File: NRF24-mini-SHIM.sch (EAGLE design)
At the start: 13 parts

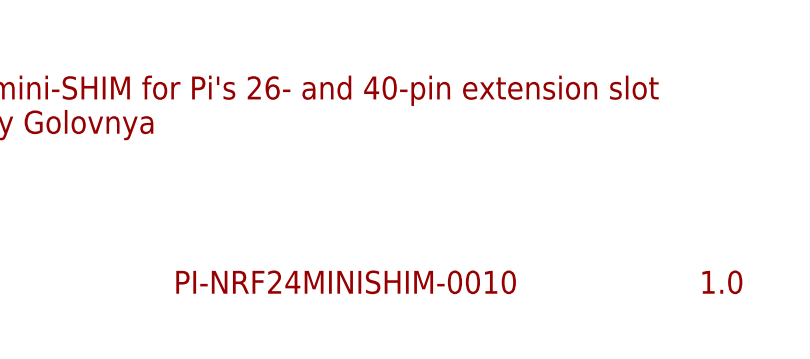
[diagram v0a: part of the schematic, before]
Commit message: Simplified document names. Generated PDF schematics.
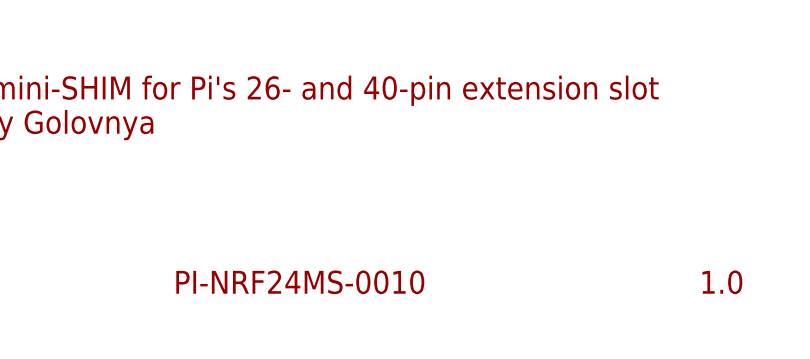
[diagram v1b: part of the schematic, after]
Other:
- note added: "PI-NRF24MS-0010"
- note removed: "PI-NRF24MINISHIM-0010"
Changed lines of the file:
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@@
 <plain>
 <text x="256.54" y="7.62" size="2.54" layer="94">1.0</text>
-<text x="198.12" y="7.62" size="2.54" layer="94">PI-NRF24MINISHIM-0010</text>
+<text x="198.12" y="7.62" size="2.54" layer="94">PI-NRF24MS-0010</text>
 <text x="165.1" y="25.4" size="2.54" layer="94">NRF24--mini-SHIM for Pi's 26- and 40-pin extension slot
 (c) Andriy Golovnya</text>
